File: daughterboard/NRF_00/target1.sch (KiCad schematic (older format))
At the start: 0 parts

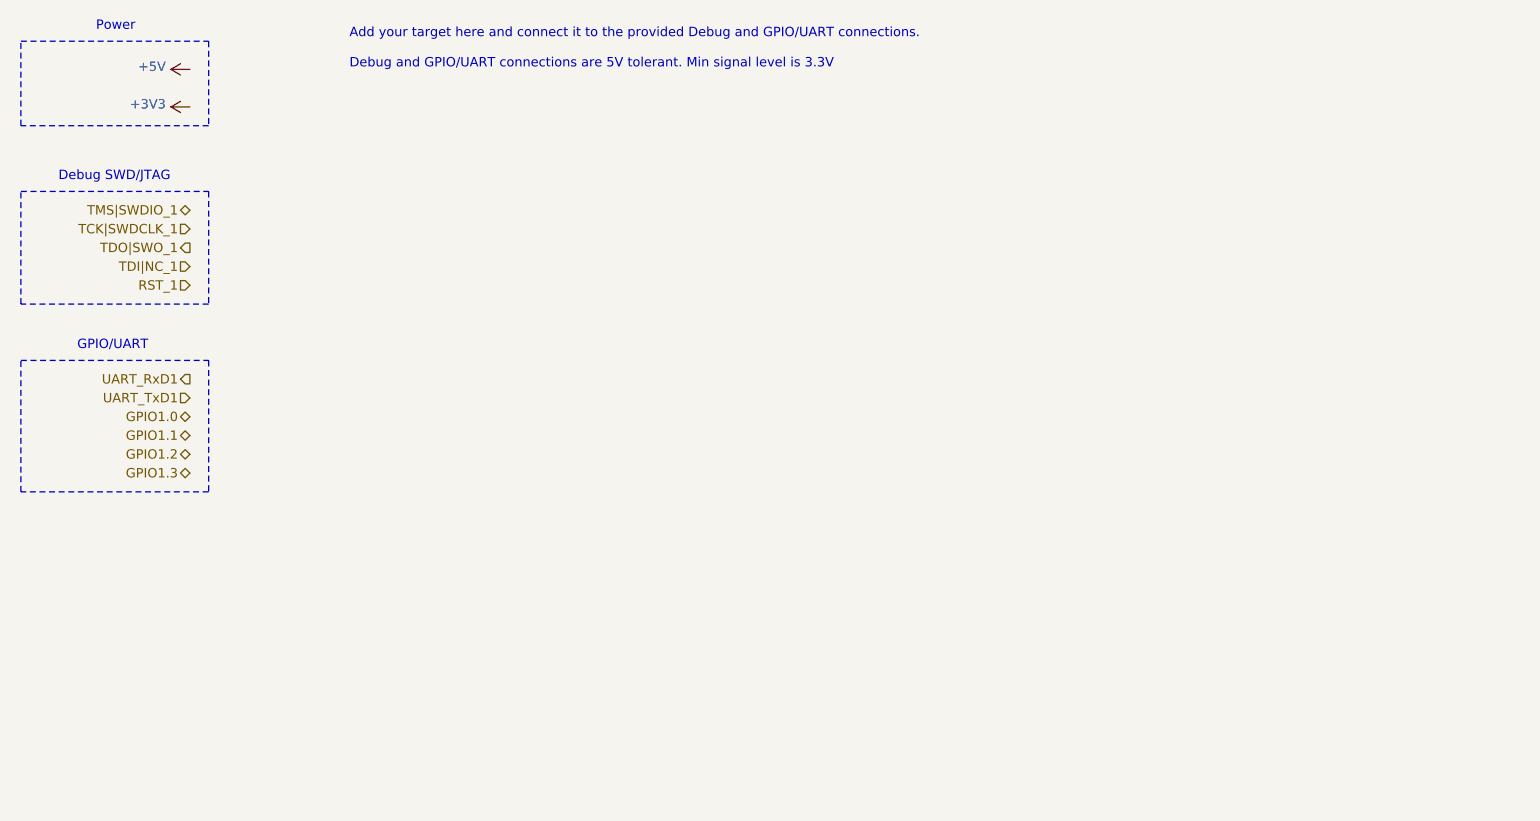
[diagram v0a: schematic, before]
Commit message: finished NRF daughterboard schematics
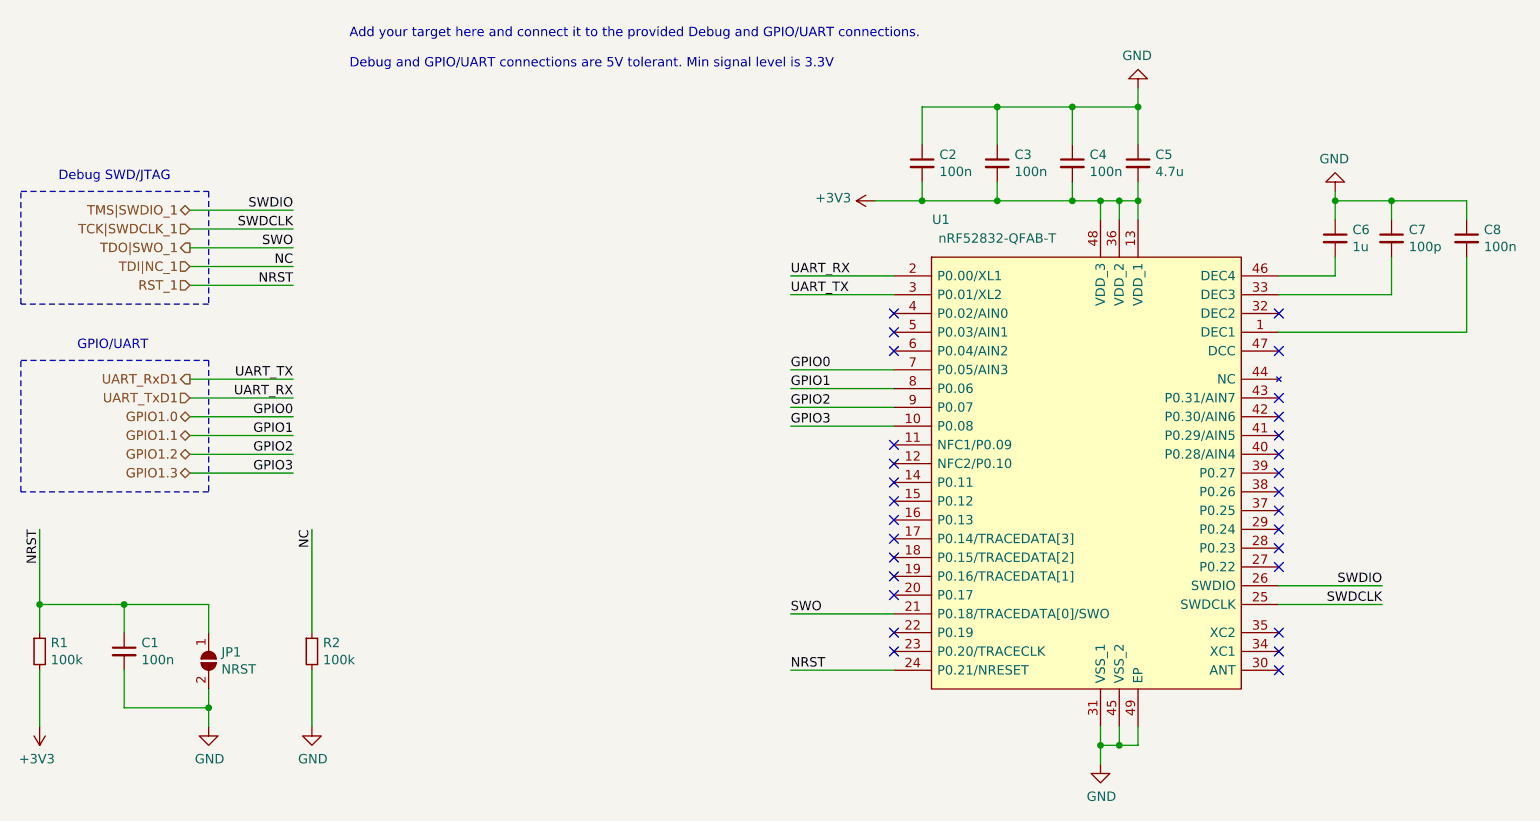
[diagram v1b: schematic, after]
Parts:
- added C1, C2, C3, C4, C8: 100n, symbol Device:C_Small
- added C5: 4.7u, symbol Device:C_Small
- added C6: 1u, symbol Device:C_Small
- added C7: 100p, symbol Device:C_Small
- added JP1: NRST, symbol Jumper:SolderJumper_2_Open
- added R1, R2: 100k, symbol Device:R_Small
- added U1: nRF52832-QFAB-T, hive_daughterboard:nRF52832-QFAB-T, symbol hive_daughterboard:nRF52832-QFAB-T
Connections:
- net +3V3: now also C2.2, C3.2, C4.2, C5.2, R1.2, U1.13 (VDD_1), U1.36 (VDD_2), U1.48 (VDD_3)
- net GPIO1.0: now also U1.7 (P0.05/AIN3)
- net GPIO1.1: now also U1.8 (P0.06)
- net GPIO1.2: now also U1.9 (P0.07)
- net GPIO1.3: now also U1.10 (P0.08)
- net RST_1: now also C1.1, JP1.1 (A), R1.1, U1.24 (P0.21/NRESET)
- net TCK|SWDCLK_1: now also U1.25 (SWDCLK)
- net TDI|NC_1: now also R2.1
- net TDO|SWO_1: now also U1.21 (P0.18/TRACEDATA[0]/SWO)
- net TMS|SWDIO_1: now also U1.26 (SWDIO)
- net UART_RxD1: now also U1.3 (P0.01/XL2)
- net UART_TxD1: now also U1.2 (P0.00/XL1)
- new net: C8.2, U1.1 (DEC1)
- new net: C7.2, U1.33 (DEC3)
- new net: C6.2, U1.46 (DEC4)
- new net GND: C1.2, C2.1, C3.1, C4.1, C5.1, C6.1, C7.1, C8.1, JP1.2 (B), R2.2, U1.31 (VSS_1), U1.45 (VSS_2), U1.49 (EP)
- no-connect marks 0 -> 29
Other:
- note removed: "Power"

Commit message: added testpoints to daughterboards, updated readme
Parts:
- added TP10: GPIO2, symbol Connector:TestPoint
- added TP11: GPIO3, symbol Connector:TestPoint
- added TP2: SWDIO, symbol Connector:TestPoint
- added TP3: SWDCLK, symbol Connector:TestPoint
- added TP4: SWO, symbol Connector:TestPoint
- added TP5: NRST, symbol Connector:TestPoint
- added TP6: UART_TX, symbol Connector:TestPoint
- added TP7: UART_RX, symbol Connector:TestPoint
- added TP8: GPIO0, symbol Connector:TestPoint
- added TP9: GPIO1, symbol Connector:TestPoint
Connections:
- net GPIO1.0: now also TP8.1
- net GPIO1.1: now also TP9.1
- net GPIO1.2: now also TP10.1
- net GPIO1.3: now also TP11.1
- net RST_1: now also TP5.1
- net TCK|SWDCLK_1: now also TP3.1
- net TDO|SWO_1: now also TP4.1
- net TMS|SWDIO_1: now also TP2.1
- net UART_RxD1: now also TP6.1
- net UART_TxD1: now also TP7.1
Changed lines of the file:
@@
 	6450 4550 6450 4650
 Connection ~ 6450 4550
+$Comp
+L Connector:TestPoint TP?
+U 1 1 6191BC6C
+P 2150 2100
+AR Path="/616688D6/6191BC6C" Ref="TP?"  Part="1"
+AR Path="/61667F91/6191BC6C" Ref="TP5"  Part="1"
+F 0 "TP5" V 2150 2300 50  0000 L CNN
+F 1 "NRST" V 2150 2650 50  0000 L CNN
+F 2 "" H 2350 2100 50  0001 C CNN
+F 3 "~" H 2350 2100 50  0001 C CNN
+	1    2150 2100
+	0    1    1    0
+$EndComp
+$Comp
+L Connector:TestPoint TP?
+U 1 1 6191BC72
+P 2150 1900
+AR Path="/616688D6/6191BC72" Ref="TP?"  Part="1"
+AR Path="/61667F91/6191BC72" Ref="TP4"  Part="1"
+F 0 "TP4" V 2150 2100 50  0000 L CNN
+F 1 "SWO" V 2150 2450 50  0000 L CNN
+F 2 "" H 2350 1900 50  0001 C CNN
+F 3 "~" H 2350 1900 50  0001 C CNN
+	1    2150 1900
+	0    1    1    0
+$EndComp
+$Comp
+L Connector:TestPoint TP?
+U 1 1 6191BC78
+P 2150 1800
+AR Path="/616688D6/6191BC78" Ref="TP?"  Part="1"
+AR Path="/61667F91/6191BC78" Ref="TP3"  Part="1"
+F 0 "TP3" V 2150 2000 50  0000 L CNN
+F 1 "SWDCLK" V 2150 2350 50  0000 L CNN
+F 2 "" H 2350 1800 50  0001 C CNN
+F 3 "~" H 2350 1800 50  0001 C CNN
+	1    2150 1800
+	0    1    1    0
+$EndComp
+$Comp
+L Connector:TestPoint TP?
+U 1 1 6191BC7E
+P 2150 1700
+AR Path="/616688D6/6191BC7E" Ref="TP?"  Part="1"
+AR Path="/61667F91/6191BC7E" Ref="TP2"  Part="1"
+F 0 "TP2" V 2150 1900 50  0000 L CNN
+F 1 "SWDIO" V 2150 2250 50  0000 L CNN
+F 2 "" H 2350 1700 50  0001 C CNN
+F 3 "~" H 2350 1700 50  0001 C CNN
+	1    2150 1700
+	0    1    1    0
+$EndComp
+$Comp
+L Connector:TestPoint TP?
+U 1 1 6191BC84
+P 2150 2600
+AR Path="/616688D6/6191BC84" Ref="TP?"  Part="1"
+AR Path="/61667F91/6191BC84" Ref="TP6"  Part="1"
+F 0 "TP6" V 2150 2800 50  0000 L CNN
+F 1 "UART_TX" V 2150 3150 50  0000 L CNN
+F 2 "" H 2350 2600 50  0001 C CNN
+F 3 "~" H 2350 2600 50  0001 C CNN
+	1    2150 2600
+	0    1    1    0
+$EndComp
+$Comp
+L Connector:TestPoint TP?
+U 1 1 6191BC8A
+P 2150 2700
+AR Path="/616688D6/6191BC8A" Ref="TP?"  Part="1"
+AR Path="/61667F91/6191BC8A" Ref="TP7"  Part="1"
+F 0 "TP7" V 2150 2900 50  0000 L CNN
+F 1 "UART_RX" V 2150 3250 50  0000 L CNN
+F 2 "" H 2350 2700 50  0001 C CNN
+F 3 "~" H 2350 2700 50  0001 C CNN
+	1    2150 2700
+	0    1    1    0
+$EndComp
+$Comp
+L Connector:TestPoint TP?
+U 1 1 6191BC90
+P 2150 2800
+AR Path="/616688D6/6191BC90" Ref="TP?"  Part="1"
+AR Path="/61667F91/6191BC90" Ref="TP8"  Part="1"
+F 0 "TP8" V 2150 3000 50  0000 L CNN
+F 1 "GPIO0" V 2150 3350 50  0000 L CNN
+F 2 "" H 2350 2800 50  0001 C CNN
+F 3 "~" H 2350 2800 50  0001 C CNN
+	1    2150 2800
+	0    1    1    0
+$EndComp
+$Comp
+L Connector:TestPoint TP?
+U 1 1 6191BC96
+P 2150 2900
+AR Path="/616688D6/6191BC96" Ref="TP?"  Part="1"
+AR Path="/61667F91/6191BC96" Ref="TP9"  Part="1"
+F 0 "TP9" V 2150 3100 50  0000 L CNN
+F 1 "GPIO1" V 2150 3450 50  0000 L CNN
+F 2 "" H 2350 2900 50  0001 C CNN
+F 3 "~" H 2350 2900 50  0001 C CNN
+	1    2150 2900
+	0    1    1    0
+$EndComp
+$Comp
+L Connector:TestPoint TP?
+U 1 1 6191BC9C
+P 2150 3000
+AR Path="/616688D6/6191BC9C" Ref="TP?"  Part="1"
+AR Path="/61667F91/6191BC9C" Ref="TP10"  Part="1"
+F 0 "TP10" V 2150 3200 50  0000 L CNN
+F 1 "GPIO2" V 2150 3550 50  0000 L CNN
+F 2 "" H 2350 3000 50  0001 C CNN
+F 3 "~" H 2350 3000 50  0001 C CNN
+	1    2150 3000
+	0    1    1    0
+$EndComp
+$Comp
+L Connector:TestPoint TP?
+U 1 1 6191BCA2
+P 2150 3100
+AR Path="/616688D6/6191BCA2" Ref="TP?"  Part="1"
+AR Path="/61667F91/6191BCA2" Ref="TP11"  Part="1"
+F 0 "TP11" V 2150 3300 50  0000 L CNN
+F 1 "GPIO3" V 2150 3650 50  0000 L CNN
+F 2 "" H 2350 3100 50  0001 C CNN
+F 3 "~" H 2350 3100 50  0001 C CNN
+	1    2150 3100
+	0    1    1    0
+$EndComp
 $EndSCHEMATC

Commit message: finished NRF daughterboard layout
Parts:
- removed TP10: GPIO2, symbol Connector:TestPoint
- removed TP11: GPIO3, symbol Connector:TestPoint
- removed TP5: NRST, symbol Connector:TestPoint
- removed TP8: GPIO0, symbol Connector:TestPoint
- removed TP9: GPIO1, symbol Connector:TestPoint
- C1, C2, C3, C4, C5, C6, C7, C8: footprint (none) -> Capacitor_SMD:C_0603_1608Metric_Pad1.05x0.95mm_HandSolder
- JP1: footprint (none) -> Jumper:SolderJumper-2_P1.3mm_Open_TrianglePad1.0x1.5mm
- R1, R2: footprint (none) -> Resistor_SMD:R_0603_1608Metric_Pad1.05x0.95mm_HandSolder
- TP2, TP3, TP4, TP6, TP7: footprint (none) -> TestPoint:TestPoint_Pad_1.0x1.0mm
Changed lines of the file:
@@
 F 0 "C6" H 7792 1896 50  0000 L CNN
 F 1 "1u" H 7792 1805 50  0000 L CNN
-F 2 "" H 7700 1850 50  0001 C CNN
+F 2 "Capacitor_SMD:C_0603_1608Metric_Pad1.05x0.95mm_HandSolder" H 7700 1850 50  0001 C CNN
 F 3 "~" H 7700 1850 50  0001 C CNN
 	1    7700 1850
@@
 F 0 "C7" H 8092 1896 50  0000 L CNN
 F 1 "100p" H 8092 1805 50  0000 L CNN
-F 2 "" H 8000 1850 50  0001 C CNN
+F 2 "Capacitor_SMD:C_0603_1608Metric_Pad1.05x0.95mm_HandSolder" H 8000 1850 50  0001 C CNN
 F 3 "~" H 8000 1850 50  0001 C CNN
 	1    8000 1850
@@
 F 0 "C8" H 8492 1896 50  0000 L CNN
 F 1 "100n" H 8492 1805 50  0000 L CNN
-F 2 "" H 8400 1850 50  0001 C CNN
+F 2 "Capacitor_SMD:C_0603_1608Metric_Pad1.05x0.95mm_HandSolder" H 8400 1850 50  0001 C CNN
 F 3 "~" H 8400 1850 50  0001 C CNN
 	1    8400 1850
@@
 F 0 "C5" H 6742 1496 50  0000 L CNN
 F 1 "4.7u" H 6742 1405 50  0000 L CNN
-F 2 "" H 6650 1450 50  0001 C CNN
+F 2 "Capacitor_SMD:C_0603_1608Metric_Pad1.05x0.95mm_HandSolder" H 6650 1450 50  0001 C CNN
 F 3 "~" H 6650 1450 50  0001 C CNN
 	1    6650 1450
@@
 F 0 "C4" H 6392 1496 50  0000 L CNN
 F 1 "100n" H 6392 1405 50  0000 L CNN
-F 2 "" H 6300 1450 50  0001 C CNN
+F 2 "Capacitor_SMD:C_0603_1608Metric_Pad1.05x0.95mm_HandSolder" H 6300 1450 50  0001 C CNN
 F 3 "~" H 6300 1450 50  0001 C CNN
 	1    6300 1450
@@
 F 0 "C3" H 5992 1496 50  0000 L CNN
 F 1 "100n" H 5992 1405 50  0000 L CNN
-F 2 "" H 5900 1450 50  0001 C CNN
+F 2 "Capacitor_SMD:C_0603_1608Metric_Pad1.05x0.95mm_HandSolder" H 5900 1450 50  0001 C CNN
 F 3 "~" H 5900 1450 50  0001 C CNN
 	1    5900 1450
@@
 F 0 "C2" H 5592 1496 50  0000 L CNN
 F 1 "100n" H 5592 1405 50  0000 L CNN
-F 2 "" H 5500 1450 50  0001 C CNN
+F 2 "Capacitor_SMD:C_0603_1608Metric_Pad1.05x0.95mm_HandSolder" H 5500 1450 50  0001 C CNN
 F 3 "~" H 5500 1450 50  0001 C CNN
 	1    5500 1450
@@
 F 0 "R1" H 859 4096 50  0000 L CNN
 F 1 "100k" H 859 4005 50  0000 L CNN
-F 2 "" H 800 4050 50  0001 C CNN
+F 2 "Resistor_SMD:R_0603_1608Metric_Pad1.05x0.95mm_HandSolder" H 800 4050 50  0001 C CNN
 F 3 "~" H 800 4050 50  0001 C CNN
 	1    800  4050
@@
 F 0 "C1" H 1342 4096 50  0000 L CNN
 F 1 "100n" H 1342 4005 50  0000 L CNN
-F 2 "" H 1250 4050 50  0001 C CNN
+F 2 "Capacitor_SMD:C_0603_1608Metric_Pad1.05x0.95mm_HandSolder" H 1250 4050 50  0001 C CNN
 F 3 "~" H 1250 4050 50  0001 C CNN
 	1    1250 4050
@@
 F 0 "JP1" V 1654 4168 50  0000 L CNN
 F 1 "NRST" V 1745 4168 50  0000 L CNN
-F 2 "" H 1700 4100 50  0001 C CNN
+F 2 "Jumper:SolderJumper-2_P1.3mm_Open_TrianglePad1.0x1.5mm" H 1700 4100 50  0001 C CNN
 F 3 "~" H 1700 4100 50  0001 C CNN
 	1    1700 4100
@@
 F 0 "R2" H 2309 4096 50  0000 L CNN
 F 1 "100k" H 2309 4005 50  0000 L CNN
-F 2 "" H 2250 4050 50  0001 C CNN
+F 2 "Resistor_SMD:R_0603_1608Metric_Pad1.05x0.95mm_HandSolder" H 2250 4050 50  0001 C CNN
 F 3 "~" H 2250 4050 50  0001 C CNN
 	1    2250 4050
@@
 $Comp
 L Connector:TestPoint TP?
-U 1 1 6191BC6C
-P 2150 2100
-AR Path="/616688D6/6191BC6C" Ref="TP?"  Part="1"
-AR Path="/61667F91/6191BC6C" Ref="TP5"  Part="1"
-F 0 "TP5" V 2150 2300 50  0000 L CNN
-F 1 "NRST" V 2150 2650 50  0000 L CNN
-F 2 "" H 2350 2100 50  0001 C CNN
-F 3 "~" H 2350 2100 50  0001 C CNN
-	1    2150 2100
-	0    1    1    0
-$EndComp
-$Comp
-L Connector:TestPoint TP?
 U 1 1 6191BC72
 P 2150 1900
@@
 F 0 "TP4" V 2150 2100 50  0000 L CNN
 F 1 "SWO" V 2150 2450 50  0000 L CNN
-F 2 "" H 2350 1900 50  0001 C CNN
+F 2 "TestPoint:TestPoint_Pad_1.0x1.0mm" H 2350 1900 50  0001 C CNN
 F 3 "~" H 2350 1900 50  0001 C CNN
 	1    2150 1900
@@
 F 0 "TP3" V 2150 2000 50  0000 L CNN
 F 1 "SWDCLK" V 2150 2350 50  0000 L CNN
-F 2 "" H 2350 1800 50  0001 C CNN
+F 2 "TestPoint:TestPoint_Pad_1.0x1.0mm" H 2350 1800 50  0001 C CNN
 F 3 "~" H 2350 1800 50  0001 C CNN
 	1    2150 1800
@@
 F 0 "TP2" V 2150 1900 50  0000 L CNN
 F 1 "SWDIO" V 2150 2250 50  0000 L CNN
-F 2 "" H 2350 1700 50  0001 C CNN
+F 2 "TestPoint:TestPoint_Pad_1.0x1.0mm" H 2350 1700 50  0001 C CNN
 F 3 "~" H 2350 1700 50  0001 C CNN
 	1    2150 1700
@@
 F 0 "TP6" V 2150 2800 50  0000 L CNN
 F 1 "UART_TX" V 2150 3150 50  0000 L CNN
-F 2 "" H 2350 2600 50  0001 C CNN
+F 2 "TestPoint:TestPoint_Pad_1.0x1.0mm" H 2350 2600 50  0001 C CNN
 F 3 "~" H 2350 2600 50  0001 C CNN
 	1    2150 2600
@@
 F 0 "TP7" V 2150 2900 50  0000 L CNN
 F 1 "UART_RX" V 2150 3250 50  0000 L CNN
-F 2 "" H 2350 2700 50  0001 C CNN
+F 2 "TestPoint:TestPoint_Pad_1.0x1.0mm" H 2350 2700 50  0001 C CNN
 F 3 "~" H 2350 2700 50  0001 C CNN
 	1    2150 2700
 	0    1    1    0
 $EndComp
-$Comp
-L Connector:TestPoint TP?
-U 1 1 6191BC90
-P 2150 2800
-AR Path="/616688D6/6191BC90" Ref="TP?"  Part="1"
-AR Path="/61667F91/6191BC90" Ref="TP8"  Part="1"
-F 0 "TP8" V 2150 3000 50  0000 L CNN
-F 1 "GPIO0" V 2150 3350 50  0000 L CNN
-F 2 "" H 2350 2800 50  0001 C CNN
-F 3 "~" H 2350 2800 50  0001 C CNN
-	1    2150 2800
-	0    1    1    0
-$EndComp
-$Comp
-L Connector:TestPoint TP?
-U 1 1 6191BC96
-P 2150 2900
-AR Path="/616688D6/6191BC96" Ref="TP?"  Part="1"
-AR Path="/61667F91/6191BC96" Ref="TP9"  Part="1"
-F 0 "TP9" V 2150 3100 50  0000 L CNN
-F 1 "GPIO1" V 2150 3450 50  0000 L CNN
-F 2 "" H 2350 2900 50  0001 C CNN
-F 3 "~" H 2350 2900 50  0001 C CNN
-	1    2150 2900
-	0    1    1    0
-$EndComp
-$Comp
-L Connector:TestPoint TP?
-U 1 1 6191BC9C
-P 2150 3000
-AR Path="/616688D6/6191BC9C" Ref="TP?"  Part="1"
-AR Path="/61667F91/6191BC9C" Ref="TP10"  Part="1"
-F 0 "TP10" V 2150 3200 50  0000 L CNN
-F 1 "GPIO2" V 2150 3550 50  0000 L CNN
-F 2 "" H 2350 3000 50  0001 C CNN
-F 3 "~" H 2350 3000 50  0001 C CNN
-	1    2150 3000
-	0    1    1    0
-$EndComp
-$Comp
-L Connector:TestPoint TP?
-U 1 1 6191BCA2
-P 2150 3100
-AR Path="/616688D6/6191BCA2" Ref="TP?"  Part="1"
-AR Path="/61667F91/6191BCA2" Ref="TP11"  Part="1"
-F 0 "TP11" V 2150 3300 50  0000 L CNN
-F 1 "GPIO3" V 2150 3650 50  0000 L CNN
-F 2 "" H 2350 3100 50  0001 C CNN
-F 3 "~" H 2350 3100 50  0001 C CNN
-	1    2150 3100
-	0    1    1    0
-$EndComp
